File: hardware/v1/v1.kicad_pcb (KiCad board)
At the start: 2 copper layers, 48 x 86 mm, 112 parts, among them J1 USB_B_Mini, J2 Conn_01x10, J3 Micro_SD_Card_Det, Q1 2N7002, Q2 DMG2301L, Q3 FDV304P, Q4 2N7002, Q5 BC817, Q6 BC817, Q7 2N7002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

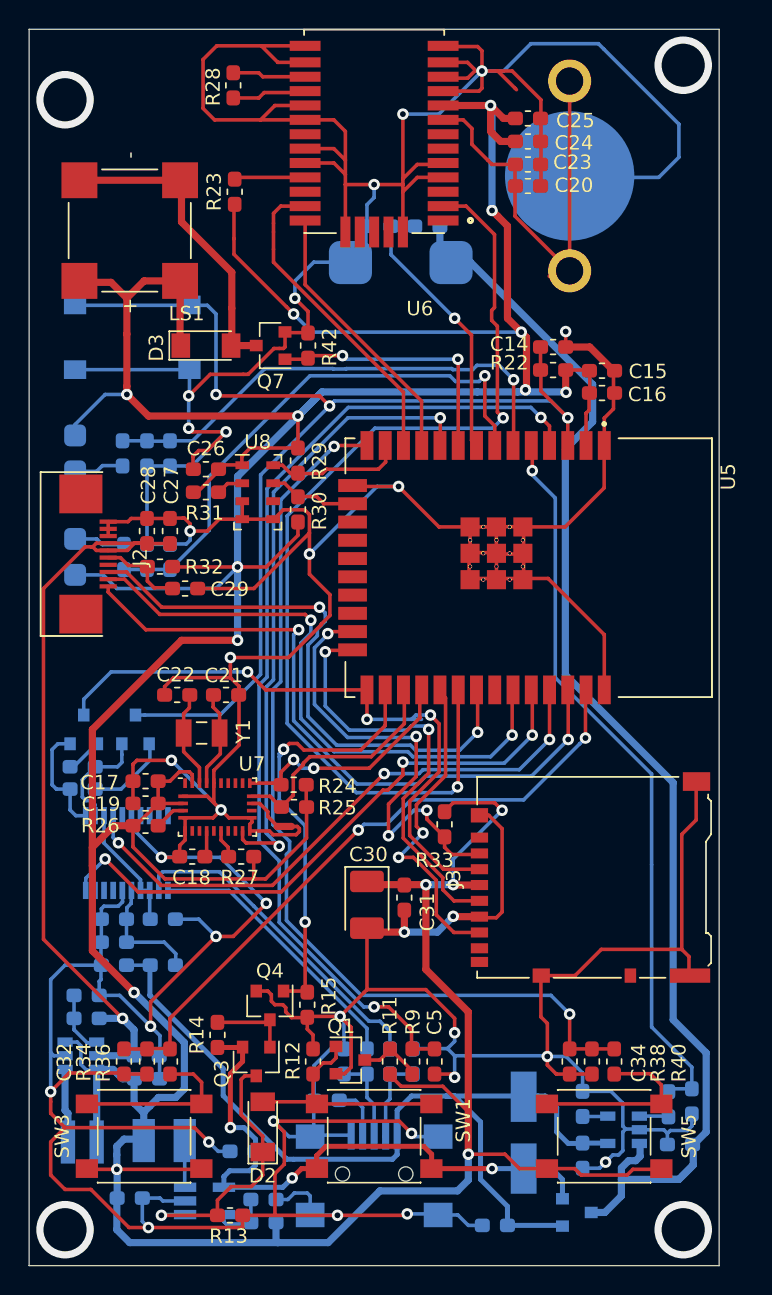
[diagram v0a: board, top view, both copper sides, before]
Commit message: Tracks sorted out, without ground plane.
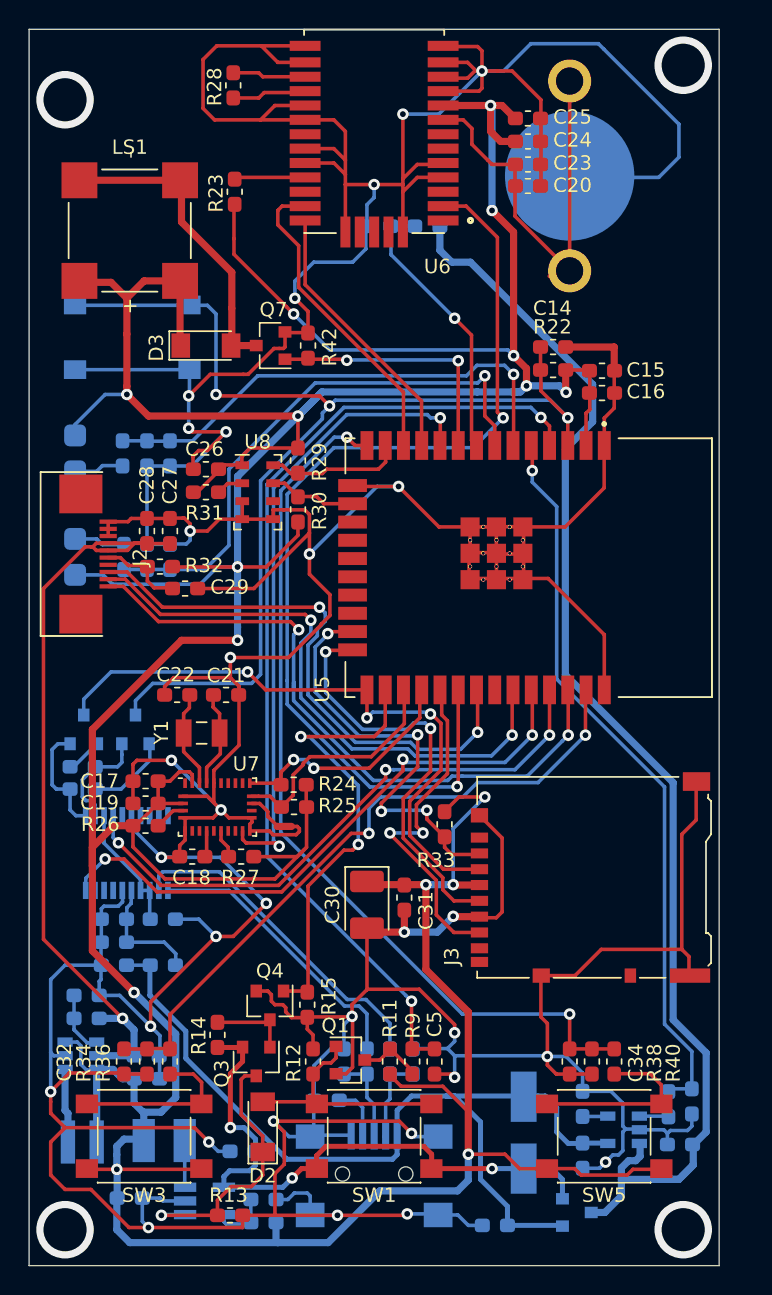
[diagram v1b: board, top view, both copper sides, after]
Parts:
- removed BT1: Li-Po, 3,7V, zmolnar-Battery:Battery_103450
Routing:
- net BT2: track 65.5 -> 62.4 mm
- net SDC-CS: track 31.3 -> 29.2 mm
- net POW-EN: track 30.5 -> 31.8 mm
- net SDC-MISO: track 22.6 -> 24.0 mm
- net nBT0: track 70.0 -> 68.7 mm
- net BT1: track 45.6 -> 46.7 mm
- net LCD-CS: track 40.2 -> 39.2 mm
- net +3V3: track 383.4 -> 384.3 mm
- net LCD-MOSI: track 41.9 -> 41.0 mm
- net Net-(R21-Pad1): track 19.2 -> 19.8 mm
- net BT4: track 38.5 -> 39.1 mm
- net GND: track 618.8 -> 618.6 mm, vias 32 -> 31

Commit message: V1.0 RC1
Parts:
- added BT1: Li-Po, 3,7V, zmolnar-Battery:Battery_103450, B.Cu at (150.0, 116.6)
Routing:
- net +BATT: track 90.8 -> 91.9 mm
- net BAT-ADC: track 19.3 -> 18.7 mm
- net GND: track 618.6 -> 618.3 mm, vias 31 -> 37
- added copper zone on B.Cu, net GND
- added copper zone on F.Cu, net GND
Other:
- board text added: "Sensorio V1.0 12/2020 zmolnar"

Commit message: V1.0 RC2
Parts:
- C27, C28: moved to B.Cu
- moved C29 5.72 mm to (135.8, 108.0)
- moved J2 5.40 mm to (129.0, 108.5)
- moved R32 4.21 mm to (133.0, 107.8), turned to 90 degrees
- moved C21 3.30 mm to (133.8, 121.6)
- moved C22 3.30 mm to (130.4, 121.6)
- moved C28 2.75 mm to (128.9, 104.2), turned to 0 degrees
- moved R31 2.71 mm to (132.1, 101.5), turned to 180 degrees
- moved C26 1.68 mm to (132.9, 104.2), turned to 90 degrees
- moved C27 1.39 mm to (128.9, 105.8), turned to 0 degrees
- moved Y1 1.35 mm to (132.1, 119.6)
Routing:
- net GND: track 618.3 -> 659.0 mm
- net LCD-SCLK: track 46.8 -> 41.4 mm
- net LCD-MOSI: track 41.0 -> 35.9 mm
- net LCD-CS: track 39.2 -> 34.4 mm
- net Net-(R31-Pad2): track 1.87 -> 5.92 mm
- net GPS-RX: track 19.1 -> 21.6 mm
- net +5V: track 54.7 -> 56.8 mm, vias 1 -> 2
- net Net-(C22-Pad2): track 6.77 -> 5.22 mm
- net Net-(C21-Pad2): track 6.72 -> 5.26 mm
- net GPS-TX: track 21.8 -> 22.8 mm
- net +3V3: track 384.3 -> 384.9 mm

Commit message: V1.0 RC3
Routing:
- net GND: vias 37 -> 80

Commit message: V1.0 final revision
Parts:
- moved R28 2.10 mm to (136.3, 75.9)
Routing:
- net Net-(R28-Pad1): track 5.11 -> 3.40 mm
- net Net-(R28-Pad2): track 5.16 -> 3.68 mm
- net LCD-CS: track 34.4 -> 33.8 mm
